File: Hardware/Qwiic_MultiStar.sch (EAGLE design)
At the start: 17 parts, among them J1 QWIIC_RIGHT_ANGLE, J2 QWIIC_RIGHT_ANGLE, J3 QWIIC_RIGHT_ANGLE, J4 QWIIC_RIGHT_ANGLE, J5 QWIIC_RIGHT_ANGLE

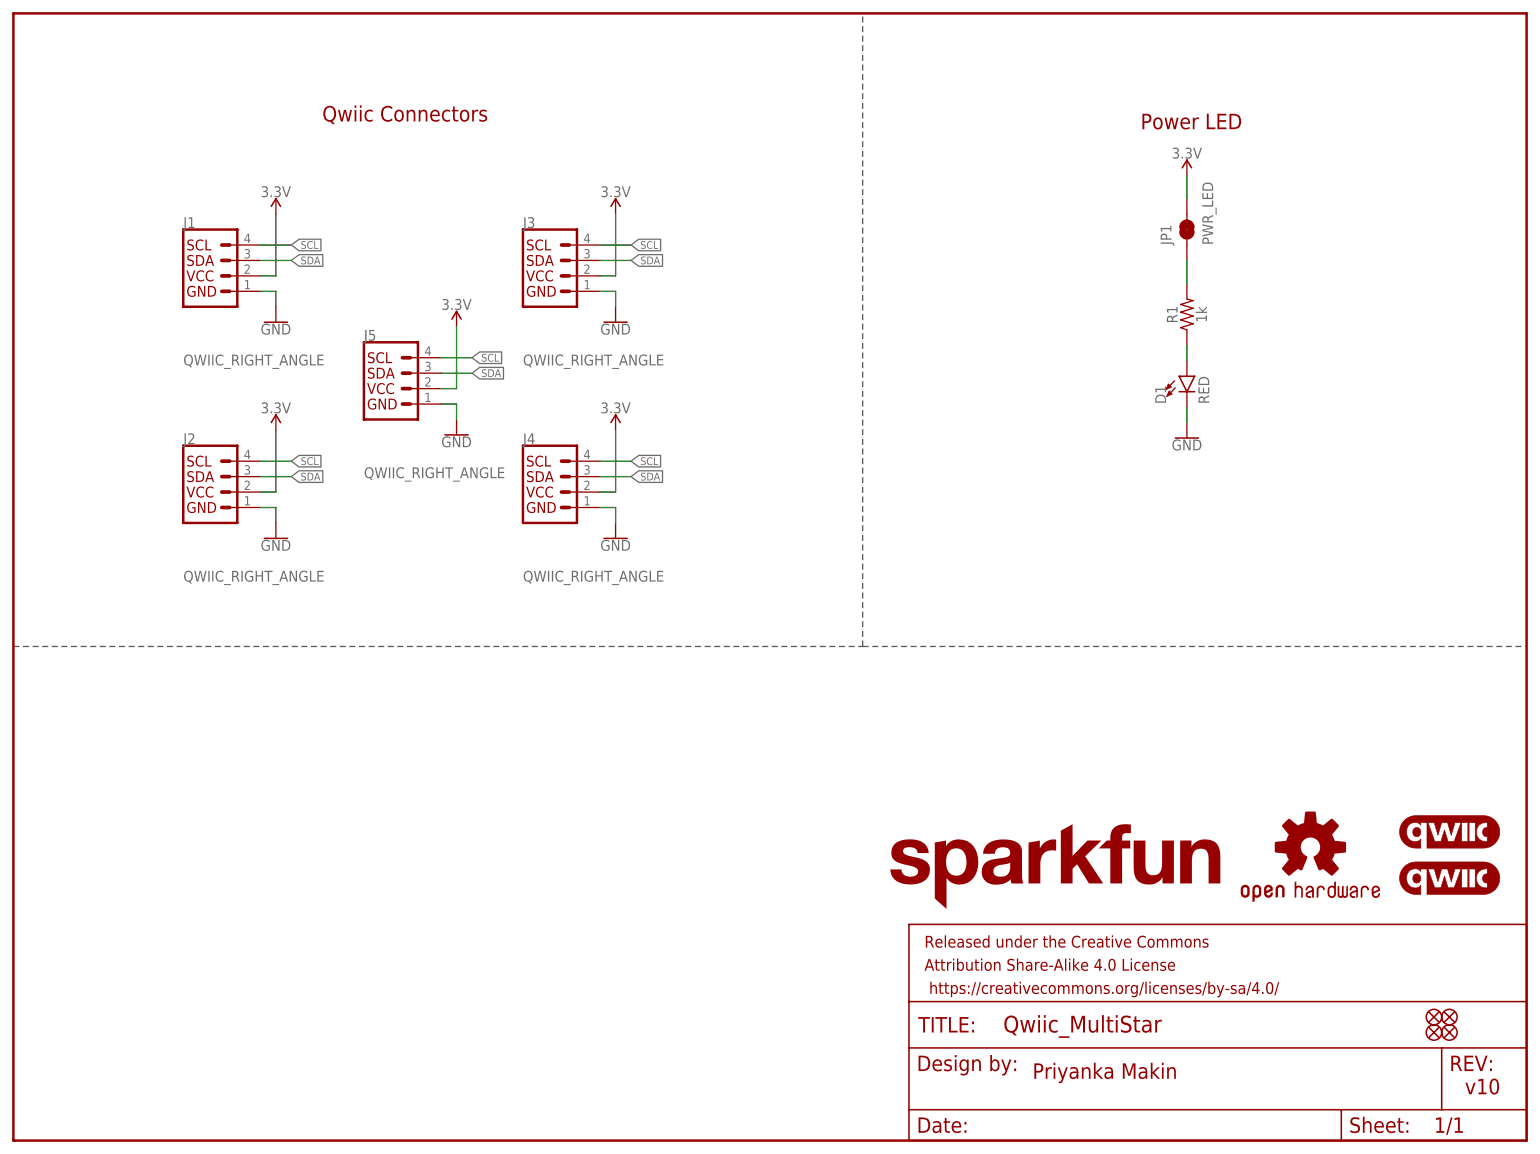
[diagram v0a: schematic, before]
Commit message: Made the dimensions symmetrical
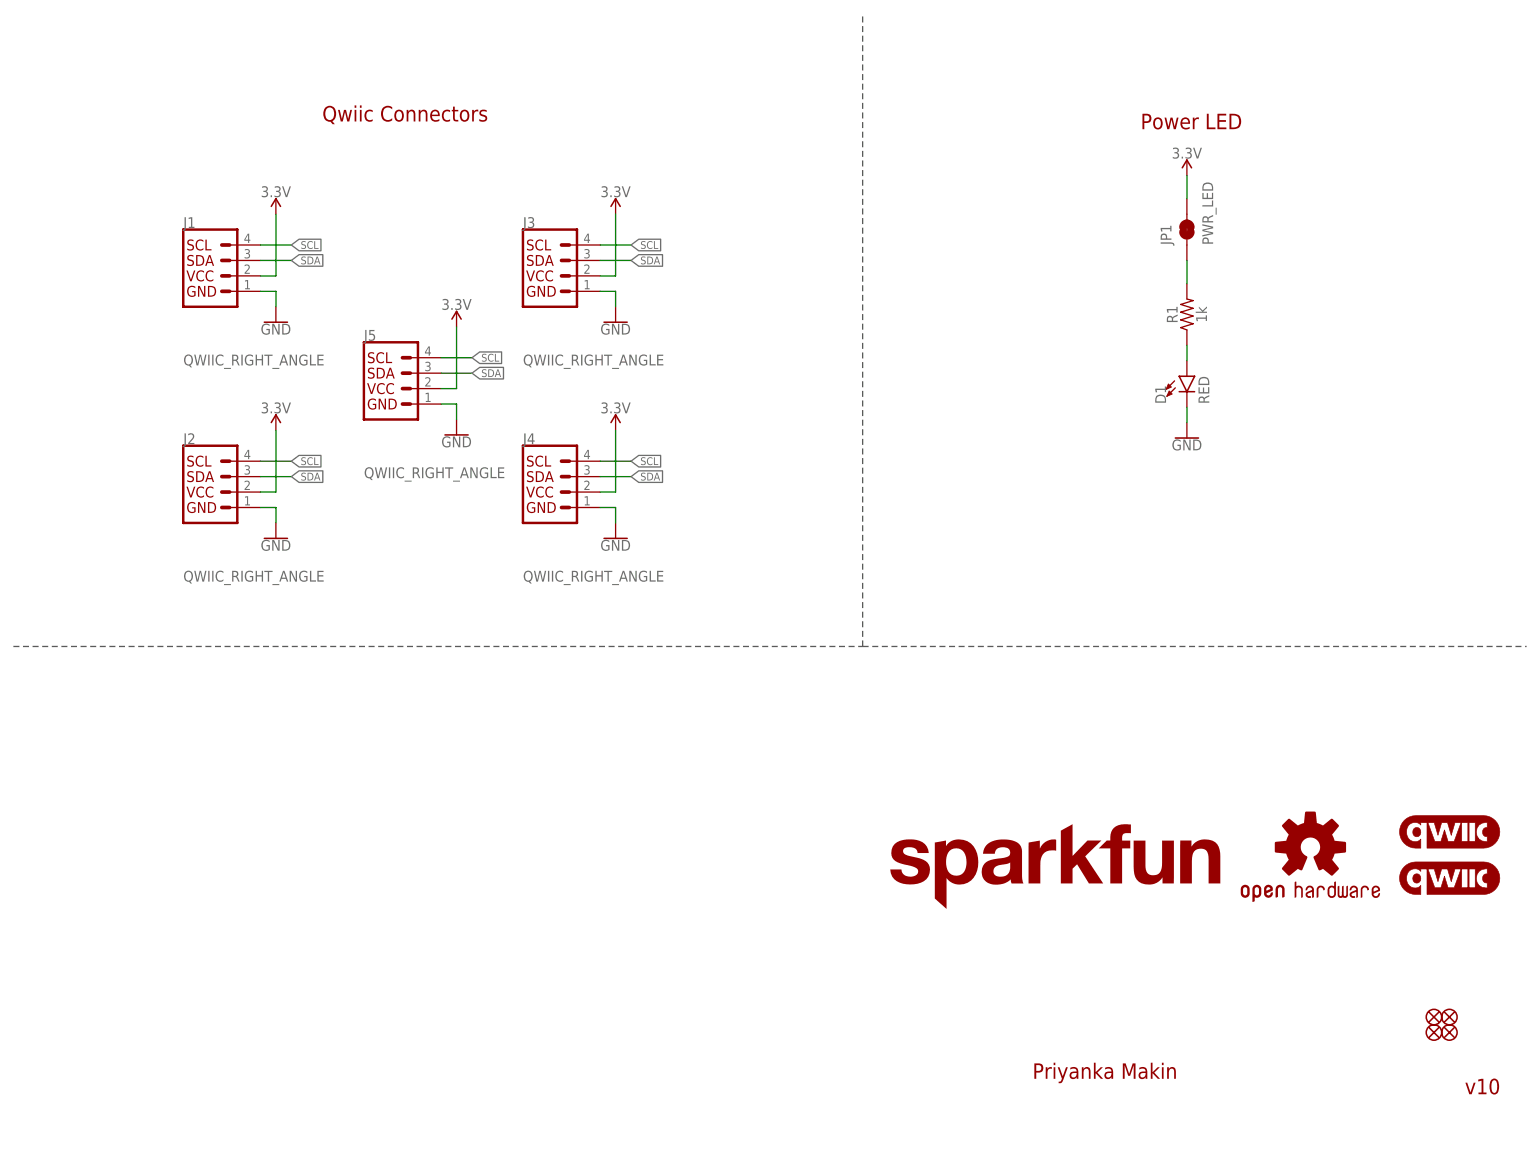
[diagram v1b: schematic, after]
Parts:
- removed FRAME1: FRAME-LETTER, SparkFun-Aesthetics:FRAME-LETTER
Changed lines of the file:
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@@
 <part name="SUPPLY3" library="SparkFun-PowerSymbols" deviceset="3.3V" device=""/>
 <part name="SUPPLY4" library="SparkFun-PowerSymbols" deviceset="3.3V" device=""/>
-<part name="FRAME1" library="SparkFun-Aesthetics" deviceset="FRAME-LETTER" device=""/>
 <part name="D1" library="SparkFun-LED" deviceset="LED-RED" device="0603" value="RED"/>
 <part name="R1" library="SparkFun-Resistors" deviceset="1KOHM" device="-0603-1/10W-1%" value="1k"/>
@@
 <attribute name="VALUE" x="99.06" y="119.634" size="1.778" layer="96" align="bottom-center"/>
 </instance>
-<instance part="FRAME1" gate="G$1" x="0" y="0" smashed="yes"/>
-<instance part="FRAME1" gate="V" x="147.32" y="0" smashed="yes">
-<attribute name="LAST_DATE_TIME" x="160.02" y="1.27" size="2.54" layer="94" font="vector"/>
-<attribute name="SHEET" x="233.68" y="1.27" size="2.54" layer="94" font="vector"/>
-<attribute name="DRAWING_NAME" x="162.814" y="17.78" size="2.7432" layer="94" font="vector"/>
-<attribute name="DESIGNER" x="170.434" y="11.176" size="2.7432" layer="94" font="vector"/>
-<attribute name="REV" x="236.22" y="6.604" size="2.7432" layer="94" font="vector"/>
-</instance>
 <instance part="D1" gate="G$1" x="193.04" y="125.73" smashed="yes">
